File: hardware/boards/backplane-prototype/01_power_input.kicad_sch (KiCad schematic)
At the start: 41 parts, among them J5 DC INPUT (GND / +VIN), U2 LM5164DDAR, U3 LM5164DDAR, U4 INA237AIDGSR

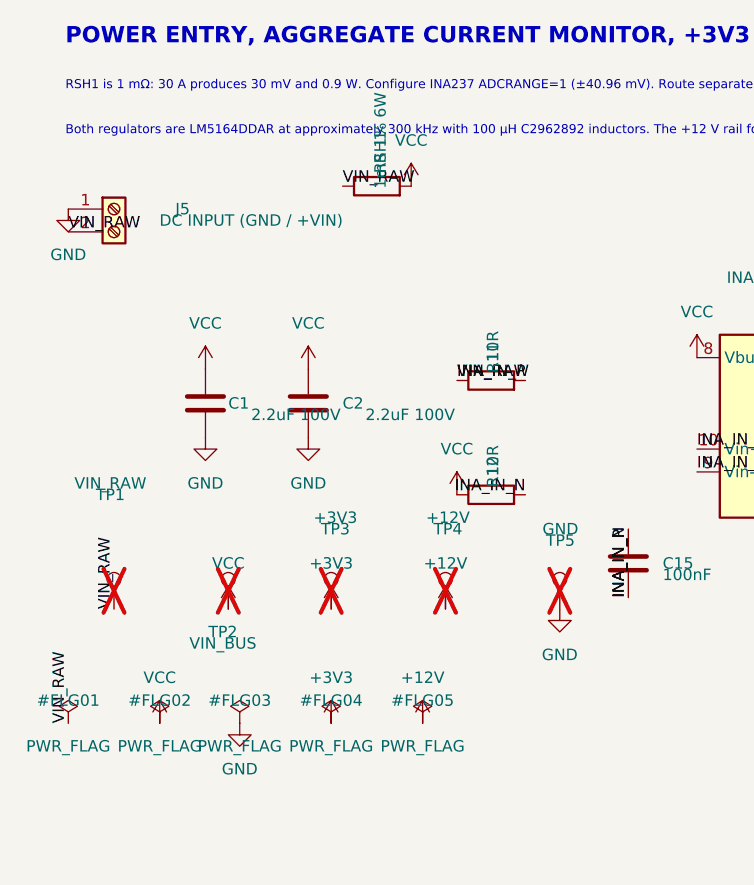
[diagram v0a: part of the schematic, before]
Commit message: use VIN_RAW power symbols throughout input sheet
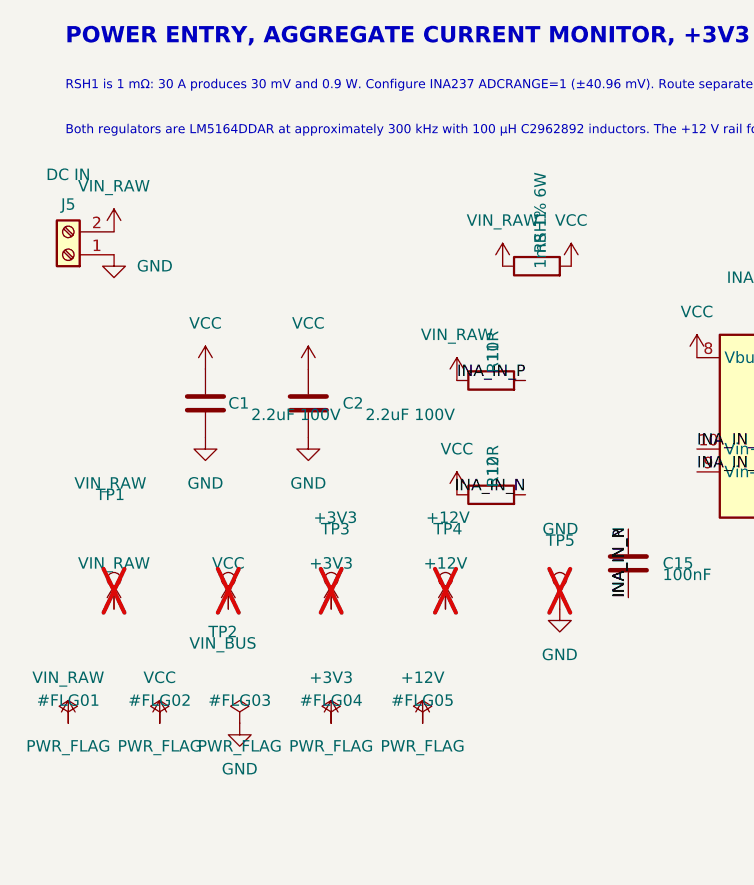
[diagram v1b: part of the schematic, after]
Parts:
- J5: value DC INPUT (GND / +VIN) -> DC IN
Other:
- moved on the sheet: J5, RSH1

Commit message: checkpoint before buck converter sheet split
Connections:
- net RON_3V3: no longer names the net of R1.1, U2.4 (RON)
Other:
- moved on the sheet: C1, C10, C11, C12, C13, C15, C16, C2, C4, C5, C6, C7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

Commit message: move buck converters to dedicated schematic sheet
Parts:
- removed C1, C2, C7, C8: 2.2uF 100V, Capacitor_SMD:C_1210_3225Metric, symbol Device:C
- removed C10, C11, C4: 22uF 25V, Capacitor_SMD:C_0805_2012Metric, symbol Device:C
- removed C12: 3.3nF 50V X7R, Capacitor_SMD:C_0603_1608Metric, symbol Device:C
- removed C13: 56pF 50V C0G, Capacitor_SMD:C_0603_1608Metric, symbol Device:C
- removed C3, C5, C9: 2.2nF 50V, Capacitor_SMD:C_0603_1608Metric, symbol Device:C
- removed C6: 220pF C0G, Capacitor_SMD:C_0603_1608Metric, symbol Device:C
- removed L1, L2: 100uH, mini-rack-power:L_PRODTech_PSPMAA0805, symbol Device:L
- removed R1: 27k 1%, Resistor_SMD:R_0603_1608Metric, symbol Device:R
- removed R10: 10k, Resistor_SMD:R_0603_1608Metric, symbol Device:R
- removed R2, R4: 110k 1%, Resistor_SMD:R_0603_1608Metric, symbol Device:R
- removed R3: 62k 1%, Resistor_SMD:R_0603_1608Metric, symbol Device:R
- removed R6: 100k 1%, Resistor_SMD:R_0603_1608Metric, symbol Device:R
- removed R7, R9: 453k 1%, Resistor_SMD:R_0603_1608Metric, symbol Device:R
- removed R8: 49.9k 1%, Resistor_SMD:R_0603_1608Metric, symbol Device:R
- removed TP3: +3V3, TestPoint:TestPoint_Pad_D1.5mm, symbol Connector:TestPoint
- removed TP4: +12V, TestPoint:TestPoint_Pad_D1.5mm, symbol Connector:TestPoint
- removed U2, U3: LM5164DDAR, Package_SO:TI_SO-PowerPAD-8, symbol mini-rack-power:LM5164DDA
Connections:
- no-connect marks 1 -> 0
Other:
- note added: "POWER ENTRY AND AGGREGATE CURRENT MONITOR"
- note added: "Verify aggregate current-sensor calibration on first articles."
- note removed: "Both regulators are LM5164DDAR at approximately 300 kHz with 100 µH C2962892 inductors. The +12 V rail follows TI's 12 V/1 A Type-3 network except for the qualified 100 µH inductor; +3V3 reuses the carrier's Type-3 values."
- note removed: "Input ceramics are 100 V rated. Add/qualify bulk input capacitance at PCB layout if the source is more than approximately 5 cm away. Verify VIN ringing, output ripple, PGOOD, inductor temperature, fan startup/stall, and current-sensor calibration on first articles."
- note removed: "POWER ENTRY, AGGREGATE CURRENT MONITOR, +3V3 AND +12V"

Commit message: checkpoint: save schematic updates
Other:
- note added: "Bypass/Pullup"
- note added: "NOTES: - RSH1 is 1 mΩ: 30 A produces 30 mV and 0.9 W. - Configure INA237 ADCRANGE=1 (±40.96 mV). LAYOUT: - Route separate Kelvin sense traces from the resistor terminals to R11/R12; do not sample from the high-current pours. TODO:r - [ ] Verify aggregate current-sensor calibration on first articles."
- note removed: "RSH1 is 1 mΩ: 30 A produces 30 mV and 0.9 W. Configure INA237 ADCRANGE=1 (±40.96 mV). Route separate Kelvin sense traces from the resistor terminals to R11/R12; do not sample from the high-current pours."
- note removed: "Verify aggregate current-sensor calibration on first articles."
- moved on the sheet: C15, C16, J5, R11, R12, R13, R14, R15, RSH1, TP1, TP2, TP5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

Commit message: Renumber backplane slot connectors J1 through J6
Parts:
- renumbered J5 to J8
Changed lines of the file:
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@@
 		(in_pos_files yes)
 		(dnp no)
-		(property "Reference" "J5"
+		(property "Reference" "J8"
 			(at 15.24 52.578 0)
 			(show_name no)
@@
 			(project "backplane-prototype"
 				(path "/348cc909-6345-4013-9bef-98714057a65b/077a6190-5781-45af-8c40-d2834d2d8f2c"
-					(reference "J5")
+					(reference "J8")
 					(unit 1)
 				)

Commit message: Resolve backplane production-preflight cleanup
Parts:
- removed TP1: VIN_RAW, TestPoint:TestPoint_Pad_D1.5mm, symbol Connector:TestPoint
- removed TP2: VIN_BUS, TestPoint:TestPoint_Pad_D1.5mm, symbol Connector:TestPoint
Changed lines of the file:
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@@
-	)
-	(junction
-		(at 68.58 58.42)
-		(diameter 0)
-		(color 0 0 0 0)
 	)
 	(junction
@@
 	(wire
 		(pts
-			(xy 68.58 58.42) (xy 66.04 58.42)
-		)
-		(stroke
-			(width 0)
-			(type default)
-		)
-	)
-	(wire
-		(pts
-			(xy 26.67 55.88) (xy 29.21 55.88)
+			(xy 72.39 58.42) (xy 66.04 58.42)
 		)
 		(stroke
@@
 		(pts
 			(xy 35.56 58.42) (xy 20.32 58.42)
-		)
-		(stroke
-			(width 0)
-			(type default)
-		)
-	)
-	(wire
-		(pts
-			(xy 72.39 58.42) (xy 68.58 58.42)
 		)
 		(stroke
@@
 	)
 	(symbol
-		(lib_id "Connector:TestPoint")
-		(at 68.58 58.42 0)
-		(mirror y)
-		(unit 1)
-		(body_style 1)
-		(exclude_from_sim no)
-		(in_bom no)
-		(on_board yes)
-		(in_pos_files yes)
-		(dnp yes)
-		(property "Reference" "TP2"
-			(at 68.58 51.816 0)
-			(show_name no)
-			(do_not_autoplace no)
-			(effects
-				(font
-					(size 1.27 1.27)
-				)
-			)
-		)
-		(property "Value" "VIN_BUS"
-			(at 69.18 62.23 0)
-			(hide yes)
-			(show_name no)
-			(do_not_autoplace no)
-			(effects
-				(font
-					(size 1.27 1.27)
-				)
-			)
-		)
-		(property "Footprint" "TestPoint:TestPoint_Pad_D1.5mm"
-			(at 64.1 58.41 0)
-			(hide yes)
-			(show_name no)
-			(do_not_autoplace no)
-			(effects
-				(font
-					(size 1.27 1.27)
-				)
-			)
-		)
-		(property "Datasheet" ""
-			(at 64.1 58.41 0)
-			(hide yes)
-			(show_name no)
-			(do_not_autoplace no)
-			(effects
-				(font
-					(size 1.27 1.27)
-				)
-			)
-		)
-		(property "Description" "test point"
-			(at 69.18 58.41 0)
-			(hide yes)
-			(show_name no)
-			(do_not_autoplace no)
-			(effects
-				(font
-					(size 1.27 1.27)
-				)
-			)
-		)
-		(pin "1"
-		)
-		(instances
-			(project "backplane-prototype"
-				(path "/348cc909-6345-4013-9bef-98714057a65b/077a6190-5781-45af-8c40-d2834d2d8f2c"
-					(reference "TP2")
-					(unit 1)
-				)
-			)
-		)
-	)
-	(symbol
 		(lib_id "power:VCC")
 		(at 35.56 78.74 0)
@@
 					(unit 1)
 				)
-			)
-		)
-	)
-	(symbol
-		(lib_id "Connector:TestPoint")
-		(at 29.21 55.88 0)
-		(unit 1)
-		(body_style 1)
-		(exclude_from_sim no)
-		(in_bom no)
-		(on_board yes)
-		(in_pos_files yes)
-		(dnp yes)
-		(property "Reference" "TP1"
-			(at 29.21 48.768 0)
-			(show_name no)
-			(do_not_autoplace no)
-			(effects
-				(font
-					(size 1.27 1.27)
-				)
-			)
-		)
-		(property "Value" "VIN_RAW"
-			(at 28.81 41.91 0)
-			(hide yes)
-			(show_name no)
-			(do_not_autoplace no)
-			(effects
-				(font
-					(size 1.27 1.27)
-				)
-			)
-		)
-		(property "Footprint" "TestPoint:TestPoint_Pad_D1.5mm"
-			(at 33.89 55.87 0)
-			(hide yes)
-			(show_name no)
-			(do_not_autoplace no)
-			(effects
-				(font
-					(size 1.27 1.27)
-				)
-			)
-		)
-		(property "Datasheet" ""
-			(at 33.89 55.87 0)
-			(hide yes)
-			(show_name no)
-			(do_not_autoplace no)
-			(effects
-				(font
-					(size 1.27 1.27)
-				)
-			)
-		)
-		(property "Description" "test point"
-			(at 28.81 55.87 0)
-			(hide yes)
-			(show_name no)
-			(do_not_autoplace no)
-			(effects
-				(font
-					(size 1.27 1.27)
-				)
-			)
-		)
-		(pin "1"
-		)
-		(instances
-			(project "backplane-prototype"
-				(path "/348cc909-6345-4013-9bef-98714057a65b/077a6190-5781-45af-8c40-d2834d2d8f2c"
-					(reference "TP1")
-					(unit 1)
-				)

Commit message: Mark backplane DC input terminal user-installed
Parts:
- J8: Population (none) -> DNP — user-installed; now not fitted
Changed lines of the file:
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@@
 		(on_board yes)
 		(in_pos_files yes)
-		(dnp no)
+		(dnp yes)
 		(property "Reference" "J8"
 			(at 15.24 52.578 0)
@@
 			(at 15.64 58.98 0)
 			(hide yes)
+			(show_name no)
+			(do_not_autoplace no)
+			(effects
+				(font
+					(size 1.27 1.27)
+				)
+			)
+		)
+		(property "Population" "DNP — user-installed"
+			(at 15.64 58.98 0)
+			(hide yes)
